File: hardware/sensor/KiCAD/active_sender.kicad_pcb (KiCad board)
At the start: 2 copper layers, 88 x 74 mm, 31 parts, among them J1 220V0, J2 Buzzer, J3 Water Sensor, Q1 AO3400A, SW1 SW_Push, SW2 SW_SPDT, U1 ESP32-C3_SUPERMINI_TH, U2 Ai-Thinker-Ra-02, U3 HLK-PM12

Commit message: dev
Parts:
- removed REF** (x4): MountingHole_2.2mm_M2_DIN965_Pad_TopOnly, MountingHole:MountingHole_2.2mm_M2_DIN965_Pad_TopOnly
- R2: value 3.9k -> 10k

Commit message: dev
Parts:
- removed DC1: Mini 560 Step-down 12V0->3V3, custom_footprints:MINI 560 PRO
- removed F1: Fuse, Fuse:Fuseholder_Cylinder-5x20mm_Schurter_0031_8201_Horizontal_Open
- removed R11, R12: 0R, Resistor_SMD:R_2512_6332Metric_Pad1.40x3.35mm_HandSolder
- added ?: , , F.Cu at (99.0, 62.0)
- added REF**: MountingHole_2.2mm_M2_DIN965_Pad, MountingHole:MountingHole_2.2mm_M2_DIN965_Pad, B.Cu at (78.0, 109.0)
- added U4: ~, custom_footprints:CKCS BS-01, B.Cu at (68.8, 72.5)
- C2: value 470u -> 100-220uF; footprint Capacitor_THT:C_Radial_D8.0mm_H11.5mm_P3.50mm -> Capacitor_SMD:C_Elec_5x5.4; moved to B.Cu
- J1: value 220V0 -> USB-C input
- U3: value HLK-PM12 -> AMS1117-3.3; footprint Converter_ACDC:Converter_ACDC_Hi-Link_HLK-PMxx -> Package_TO_SOT_SMD:SOT-223-3_TabPin2; moved to B.Cu
- moved J1 54.9 mm to (80.0, 66.5)
- moved R9 47.3 mm to (79.5, 85.5)
- moved R5 46.4 mm to (79.5, 90.0), turned to 0 degrees
- moved C1 36.1 mm to (76.5, 122.5), turned to 180 degrees
- moved R4 36.0 mm to (79.0, 118.5), turned to 0 degrees
- moved R3 35.4 mm to (79.0, 114.5), turned to 180 degrees
- moved R1 29.0 mm to (78.5, 100.0)
- moved C2 27.9 mm to (108.8, 75.0), turned to 180 degrees
- moved D1 27.6 mm to (67.0, 102.5)
- moved J2 27.6 mm to (69.0, 96.5)
- moved R7 27.5 mm to (87.5, 100.0)
- moved R6 27.5 mm to (87.5, 93.5)
- moved U1 27.2 mm to (104.5, 109.3)
- moved U2 27.2 mm to (103.0, 80.5)
- moved SW2 27.2 mm to (63.9, 109.5)
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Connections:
- C2 pad 1: /12V0 -> GNDD
- C2 pad 2: GNDPWR -> +3.3V
- D1 pad 1: /12V0 -> +12V
- J1 pad 1: Net-(J1-Pin_1) -> +5V
- J1 pad 2: /N 220V0 -> GNDD
- J2 pad 2: /12V0 -> +12V
- J3 pad 1: /12V0 -> +5V
- J3 pad 3: GNDPWR -> GNDD
- Q1 pad 2: GNDPWR -> GNDD
- R2 pad 2: GNDD -> +3.3V
- R5 pad 2: GNDPWR -> GNDD
- SW2 pad 1: GNDPWR -> GNDD
- SW2 pad 3: /12V0 -> +5V
- U3 pad 1: /220V0 -> GNDD
- U3 pad 2: /N 220V0 -> +3.3V
- U3 pad 3: GNDPWR -> +5V
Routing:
- net +5V: track 0.00 -> 96.0 mm
- net /12V0: track 92.9 -> 0.00 mm
- net Net-(R4-Pad2): track 50.6 -> 10.4 mm
- net GNDD: track 38.3 -> 0.00 mm, vias 0 -> 4
- net /N 220V0: track 29.3 -> 0.00 mm
- net +12V: track 0.00 -> 24.5 mm
- net +3.3V: track 84.1 -> 97.0 mm
- net Net-(J1-Pin_1): track 10.2 -> 0.00 mm
- net Net-(R6-Pad1): track 0.00 -> 9.67 mm
- net Net-(Q1-G): track 16.2 -> 8.96 mm
- net /220V0: track 6.91 -> 0.00 mm
- net /LINK_BUTTON: track 53.9 -> 59.4 mm
- net Net-(D1-A): track 11.9 -> 16.0 mm
- net Net-(R1-Pad2): track 12.1 -> 8.80 mm
- net /LORA_RESET: track 42.3 -> 40.2 mm
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- added copper zone on F.Cu, net GNDD
- removed copper zone on B.Cu, net GNDPWR
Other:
- board size 88 x 74 mm -> 63 x 70 mm

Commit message: dev
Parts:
- R2, R5, R8: value 10k -> 10k,1206
- R3: value 10k,0603 -> 10k,1206
- R4, R9: value 330 -> 330,1206

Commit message: dev
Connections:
- U4 pad 1: +5V -> GNDD
- U4 pad 2: GNDD -> +5V

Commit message: dev
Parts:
- removed R1: 10k, Resistor_SMD:R_1206_3216Metric_Pad1.30x1.75mm_HandSolder
- removed R10, R13, R7: 0R, Resistor_SMD:R_2512_6332Metric_Pad1.40x3.35mm_HandSolder
- removed R8: 10k,1206, Resistor_SMD:R_1206_3216Metric_Pad1.30x1.75mm_HandSolder
- removed U2: Ai-Thinker-Ra-02, custom_footprints:Ai-Thinker-Ra-01-LoRa BREAKOUT BOARD
- added BT1: Battery, custom_footprints:BHC-CR123A, B.Cu at (98.0, 102.0)
- added BZ1: Buzzer, Buzzer_Beeper:Buzzer_12x9.5RM7.6, B.Cu at (98.0, 76.0)
- added C4: 0805,47uF, Capacitor_SMD:C_0805_2012Metric_Pad1.18x1.45mm_HandSolder, F.Cu at (74.0, 91.5)
- added C5: 0805,47uF (min 10V), Capacitor_SMD:C_0805_2012Metric_Pad1.18x1.45mm_HandSolder, F.Cu at (65.1, 111.0)
- added C6: 47uF, Capacitor_SMD:C_0805_2012Metric_Pad1.18x1.45mm_HandSolder, F.Cu at (83.2, 91.8)
- added C7: 47uF, Capacitor_SMD:C_0805_2012Metric_Pad1.18x1.45mm_HandSolder, F.Cu at (89.8, 97.5)
- added C8: 0,1uF, Capacitor_SMD:C_0805_2012Metric_Pad1.18x1.45mm_HandSolder, F.Cu at (68.5, 75.5)
- added C9: 100uF, Capacitor_SMD:C_0805_2012Metric_Pad1.18x1.45mm_HandSolder, F.Cu at (77.5, 82.2)
- added D2: SS14, Diode_SMD:D_SMA, F.Cu at (71.5, 104.5)
- added L1: 47uH, CDRH74, Inductor_SMD:L_7.3x7.3_H4.5, F.Cu at (68.0, 96.0)
- added Q2: AO3401A, Package_TO_SOT_SMD:SOT-23, F.Cu at (93.0, 91.0)
- added Q3: AO3401A, Package_TO_SOT_SMD:SOT-23, F.Cu at (77.5, 96.1)
- added R11: 100k,1206, Resistor_SMD:R_1206_3216Metric_Pad1.30x1.75mm_HandSolder, F.Cu at (97.8, 99.0)
- added R12: 10k, Resistor_SMD:R_1206_3216Metric_Pad1.30x1.75mm_HandSolder, F.Cu at (94.5, 72.8)
- C1, D1, Q1, R2, R4, R5, R9, U3: moved to F.Cu
- C2: value 100-220uF -> 100uF; footprint Capacitor_SMD:C_Elec_5x5.4 -> Capacitor_SMD:C_0805_2012Metric_Pad1.18x1.45mm_HandSolder; moved to F.Cu
- J1: value USB-C input -> Conn_01x04_Pin; footprint TerminalBlock_Phoenix:TerminalBlock_Phoenix_MKDS-1,5-2_1x02_P5.00mm_Horizontal -> Connector_PinHeader_2.00mm:PinHeader_1x05_P2.00mm_Vertical; moved to B.Cu
- J2: value Buzzer -> USB-C connector; footprint TerminalBlock_Phoenix:TerminalBlock_Phoenix_MKDS-1,5-2_1x02_P5.00mm_Horizontal -> Connector_JST:JST_PH_B2B-PH-K_1x02_P2.00mm_Vertical; moved to B.Cu
- J3, SW1, SW2: moved to B.Cu
- R3: value 10k,1206 -> 100k,1206; moved to F.Cu
- R6: value 0R -> 100k,1206; footprint Resistor_SMD:R_2512_6332Metric_Pad1.40x3.35mm_HandSolder -> Resistor_SMD:R_1206_3216Metric_Pad1.30x1.75mm_HandSolder; moved to F.Cu
- U1: value ESP32-C3_SUPERMINI_TH -> HT7750_C250900; footprint custom_footprints:MODULE_ESP32-C3_SUPERMINI_TH -> custom_footprints:HT7750
- U4: value ~ -> E77-900M22S; footprint custom_footprints:CKCS BS-01 -> custom_footprints:COMM-SMD_30P-L20.0-W14.0-P1.27; moved to F.Cu
- moved C2 41.9 mm to (68.5, 63.5), turned to -90 degrees
- moved U1 40.7 mm to (64.1, 104.9), turned to 90 degrees
- moved Q1 33.8 mm to (94.5, 65.5)
- moved R5 33.3 mm to (99.0, 63.0), turned to 90 degrees
- moved C1 27.8 mm to (103.0, 114.0)
- moved R3 25.4 mm to (103.0, 106.0), turned to 0 degrees
- moved R4 25.4 mm to (103.0, 110.0), turned to 180 degrees
- moved J2 24.1 mm to (92.8, 100.5)
- moved R2 23.0 mm to (65.5, 88.0), turned to 180 degrees
- moved D1 19.8 mm to (80.5, 88.0)
- moved R9 19.7 mm to (91.0, 69.5), turned to 90 degrees
- moved J1 18.6 mm to (64.2, 76.4), turned to 180 degrees
- moved U3 18.6 mm to (84.2, 98.8), turned to 90 degrees
- moved SW2 15.1 mm to (77.0, 117.0), turned to 90 degrees
- moved R6 13.2 mm to (77.4, 102.0), turned to 180 degrees
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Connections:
- C2 pad 1: GNDD -> /NRST
- C2 pad 2: +3.3V -> GNDD
- D1 pad 1: +12V -> +3.3V
- J1 pad 1: +5V -> +3.3V
- J1 pad 2: GNDD -> /SWDIO
- J2 pad 1: Net-(D1-A) -> GNDD
- J2 pad 2: +12V -> +5V
- J3 pad 2: Net-(J3-Pin_2) -> /SENSOR
- Q1 pad 1: Net-(Q1-G) -> /BUZZER
- Q1 pad 3: Net-(D1-A) -> Net-(Q1-D)
- R2 pad 1: Net-(R1-Pad2) -> +3.3V
- R2 pad 2: +3.3V -> /SENSOR
- R5 pad 1: Net-(Q1-G) -> /BUZZER
- R6 pad 1: Net-(R6-Pad1) -> +3.3V
- R6 pad 2: /BUZZER -> /HT7750_EN
- R9 pad 1: Net-(Q1-G) -> Net-(BZ1--)
- R9 pad 2: Net-(R6-Pad1) -> Net-(Q1-D)
- SW1 pad 1: Net-(R4-Pad2) -> GNDD
- SW1 pad 2: GNDD -> Net-(R4-Pad2)
- SW2 pad 2: Net-(SW2-B) -> /MODE
- U1 pad 1: /SENSOR -> GNDD
- U1 pad 2: unconnected-(U1-GPIO2-Pad2) -> +5V
- U1 pad 3: /LORA_RESET -> Net-(D2-A)
- U3 pad 2: +3.3V -> Net-(D1-A)
- U4 pad 1: GNDD -> /BUZZER
- U4 pad 2: +5V -> unconnected-(U4-PB4-Pad2)
- U4 pad 3: +12V -> unconnected-(U4-PB5-Pad3)
- U4 pad 4: GNDD -> unconnected-(U4-PB6-Pad4)
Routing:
- net /SENSOR: track 7.75 -> 101.3 mm
- net /HT7750_EN: track 0.00 -> 78.8 mm
- net /LORA_DIO0: track 59.7 -> 0.00 mm
- net /LORA_RESET: track 40.2 -> 0.00 mm
- net /LORA_MISO: track 31.6 -> 0.00 mm
- net /NRST: track 0.00 -> 31.2 mm
- net /LORA_NSS: track 30.5 -> 0.00 mm
- net /LORA_MOSI: track 27.1 -> 0.00 mm
- net Net-(J3-Pin_2): track 26.5 -> 0.00 mm
- net +5V: track 96.1 -> 70.4 mm
- net +12V: track 24.5 -> 0.00 mm
- net +3.3V: track 97.0 -> 118.8 mm
- net /LORA_SCK: track 21.6 -> 0.00 mm
- net /BUZZER: track 10.5 -> 30.6 mm
- net /LINK_BUTTON: track 59.4 -> 77.1 mm
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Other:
- board size 63 x 70 mm -> 55.5 x 70 mm

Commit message: dev
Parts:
- moved ? 40.4 mm to (66.8, 69.2)
- moved J2 11.7 mm to (84.2, 108.5)
- moved R11 6.05 mm to (93.0, 102.8), turned to 180 degrees
- moved J3 1.80 mm to (70.5, 117.0)
- moved D2 1.00 mm to (70.5, 104.5)
- moved R5 1.00 mm to (98.0, 63.0)
- moved SW2 1.00 mm to (76.0, 117.0)
- moved SW1 0.75 mm to (86.2, 114.5)
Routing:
- net /SENSOR: track 101.3 -> 99.3 mm
- net +3.3V: track 118.8 -> 117.4 mm
- net /BUZZER: track 30.6 -> 29.6 mm
- net Net-(R4-Pad2): track 24.6 -> 25.4 mm
- net Net-(BT1-+): track 9.51 -> 8.78 mm
- net +5V: track 70.4 -> 71.1 mm
- net Net-(D2-A): track 14.6 -> 15.2 mm
- net /MODE: track 18.7 -> 18.2 mm
- net GNDD: vias 8 -> 9
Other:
- board size 55.5 x 70 mm -> 50 x 70 mm

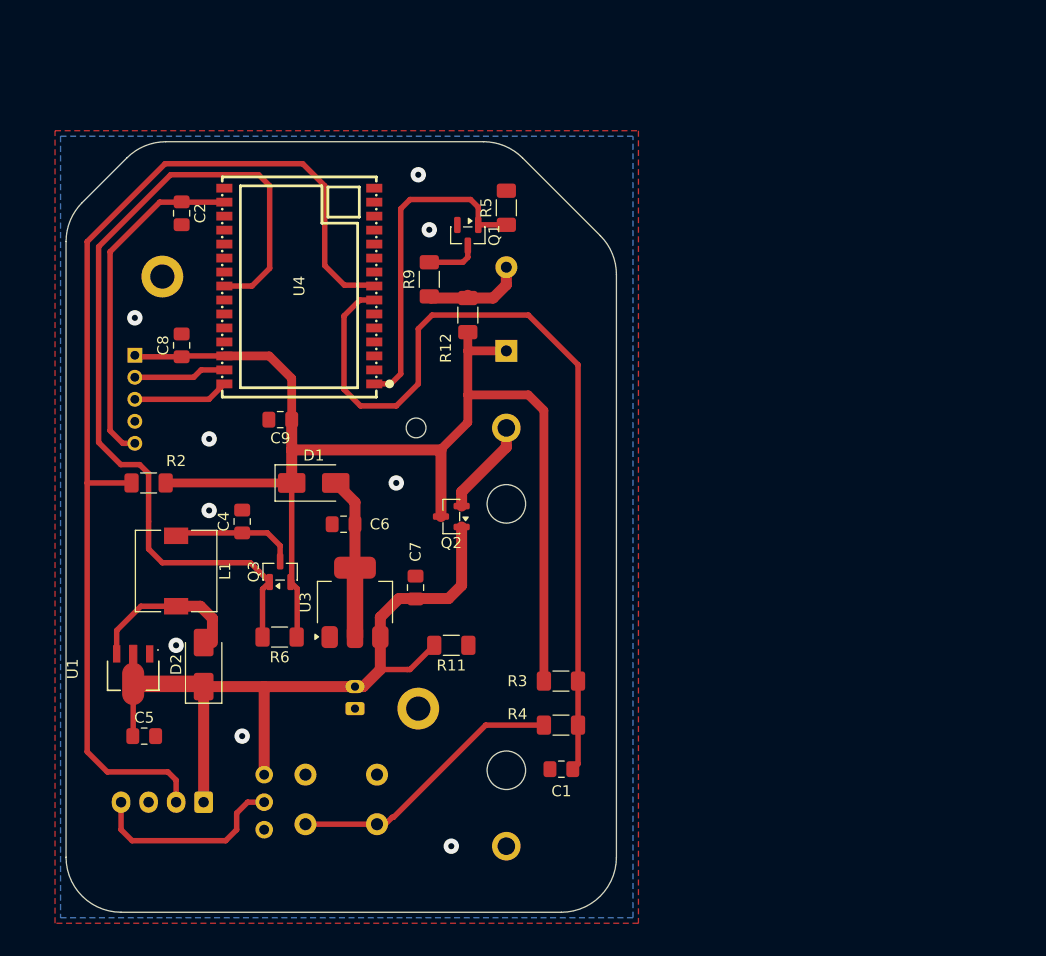
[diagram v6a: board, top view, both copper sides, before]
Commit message: added alarm acknowledge and many code improvements
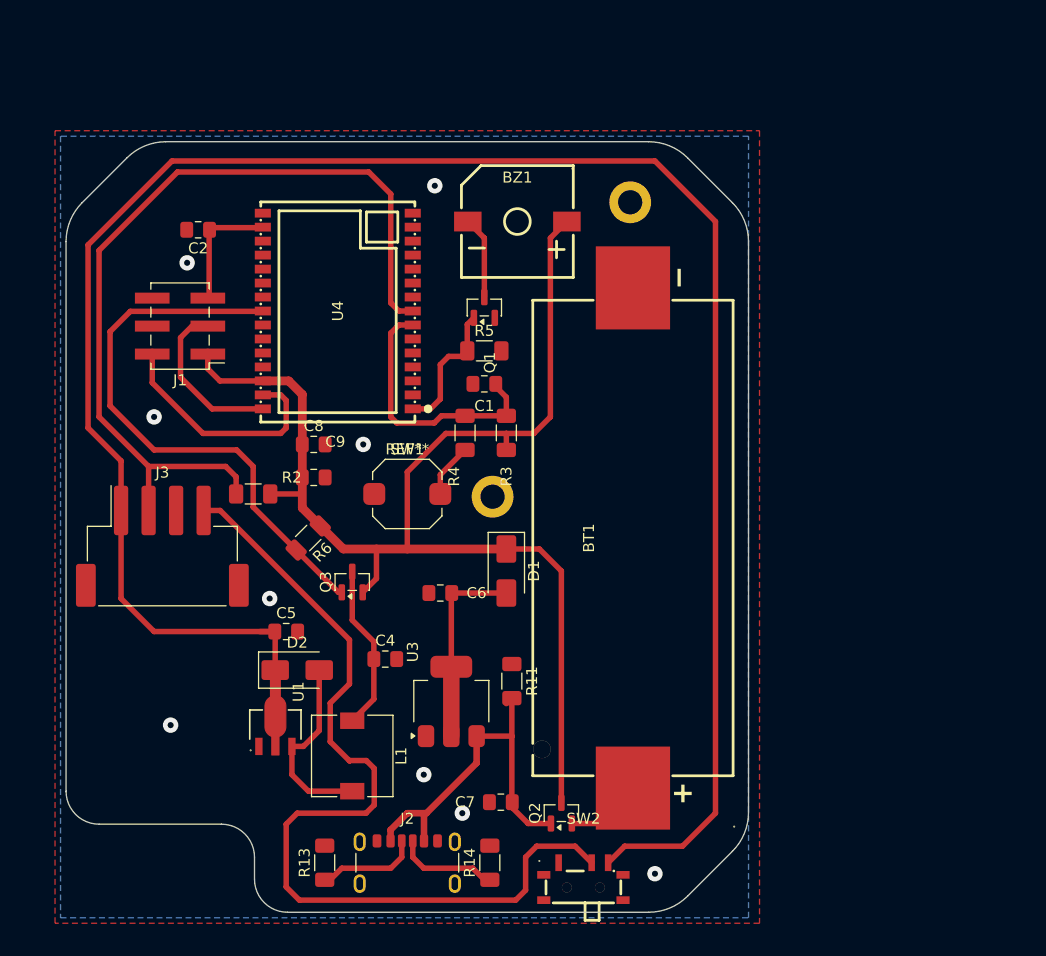
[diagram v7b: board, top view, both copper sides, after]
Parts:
- removed R12: 10k, Resistor_SMD:R_1206_3216Metric_Pad1.30x1.75mm_HandSolder
- removed R9: 330,1206, Resistor_SMD:R_1206_3216Metric_Pad1.30x1.75mm_HandSolder
- added R13: 5.1k,1206, Resistor_SMD:R_1206_3216Metric_Pad1.30x1.75mm_HandSolder, F.Cu at (81.5, 122.5)
- added R14: 5.1k,1206, Resistor_SMD:R_1206_3216Metric_Pad1.30x1.75mm_HandSolder, F.Cu at (96.5, 122.5)
- BT1: footprint custom_footprints:BHC-CR123A -> custom_footprints:CR123A-SMD_BH-123A-B5BA003; moved to F.Cu
- BZ1: footprint Buzzer_Beeper:Buzzer_12x9.5RM7.6 -> custom_footprints:Huaneng MLT-9650; moved to F.Cu
- J1: footprint Connector_PinHeader_2.00mm:PinHeader_1x05_P2.00mm_Vertical -> Connector_PinHeader_2.54mm:PinHeader_2x03_P2.54mm_Vertical_SMD; moved to F.Cu
- J2: value USB-C connector -> USB_C_Receptacle_PowerOnly_6P; footprint Connector_JST:JST_PH_B2B-PH-K_1x02_P2.00mm_Vertical -> Connector_USB:USB_C_Receptacle_GCT_USB4125-xx-x-0190_6P_TopMnt_Horizontal; moved to F.Cu
- J3: footprint Connector_JST:JST_XH_S4B-XH-A-1_1x04_P2.50mm_Horizontal -> Connector_JST:JST_XH_S4B-XH-SM4-TB_1x04-1MP_P2.50mm_Horizontal; moved to F.Cu
- SW1: footprint Button_Switch_THT:SW_PUSH_6mm_H5mm -> Button_Switch_SMD:SW_Push_1TS009xxxx-xxxx-xxxx_6x6x5mm; moved to F.Cu
- SW2: footprint custom_footprints:SS12D00 -> custom_footprints:MSK12-C02; moved to F.Cu
- moved ? 43.0 mm to (109.2, 62.5)
- moved C1 35.7 mm to (96.0, 79.0)
- moved SW2 29.9 mm to (105.0, 124.2), turned to 0 degrees
- moved Q2 28.7 mm to (103.0, 118.0), turned to 90 degrees
- moved R4 27.9 mm to (94.2, 83.5), turned to -90 degrees
- moved SW1 25.6 mm to (89.0, 89.0), turned to 0 degrees
- moved J3 23.6 mm to (66.8, 93.8), turned to 0 degrees
- moved L1 23.2 mm to (84.0, 112.8)
- moved R3 23.1 mm to (98.0, 83.5), turned to 90 degrees
- moved C7 21.0 mm to (97.5, 117.0), turned to 180 degrees
- moved REF** 20.4 mm to (96.8, 89.2)
- moved D1 19.2 mm to (98.0, 96.0), turned to -90 degrees
- moved C4 18.0 mm to (87.0, 104.0), turned to 0 degrees
- moved C5 16.0 mm to (78.0, 101.5)
- moved J2 15.8 mm to (89.0, 123.6), turned to 0 degrees
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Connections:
- BZ1 pad 2: Net-(BZ1--) -> Net-(Q1-D)
- C5 pad 1: +5V -> /SENSOR_5V
- C7 pad 1: +5V -> Net-(Q2-G)
- D2 pad 1: +5V -> /SENSOR_5V
- J3 pad 1: +5V -> /SENSOR_5V
- Q2 pad 1: +5V -> Net-(Q2-G)
- R11 pad 2: +5V -> Net-(Q2-G)
- SW2 pad 3: +5V -> /SENSOR_5V
- U1 pad 2: +5V -> /SENSOR_5V
- U3 pad 3: +5V -> Net-(Q2-G)
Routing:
- net /SENSOR_5V: track 0.00 -> 185.4 mm
- net +5V: track 71.1 -> 0.00 mm
- net /MODE: track 18.2 -> 83.5 mm
- net /LINK_BUTTON: track 77.1 -> 24.0 mm
- net Net-(Q2-G): track 0.00 -> 34.2 mm
- net /HT7750_EN: track 78.8 -> 51.6 mm
- net /SENSOR: track 99.3 -> 77.9 mm
- net Net-(R4-Pad2): track 25.4 -> 4.93 mm
- net /NRST: track 31.2 -> 11.1 mm
- net /BUZZER: track 29.6 -> 12.2 mm
- net /SWDIO: track 8.41 -> 22.0 mm
- net Net-(BZ1--): track 9.16 -> 0.00 mm
- net Net-(J2-CC2): track 0.00 -> 8.83 mm
- net Net-(J2-CC1): track 0.00 -> 8.83 mm
- net /SWCLK: track 8.71 -> 15.2 mm
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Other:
- board size 50 x 70 mm -> 62 x 70 mm
